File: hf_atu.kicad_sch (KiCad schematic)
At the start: 112 parts, among them J10 TO SWR_IN, J11 TO FILT_OUT, J7 To CTRL:ATU, J8 SWR_IN, J9 TO ANTENNA, K12 G6E, K13 G6E, K14 G6E, K15 G6E, K16 G6E, K17 G6E, K18 G6E, K19 G6E, K20 G6E, K21 G6E, K22 G6E, K23 G6E, K24 G6E, K25 G6E, K26 G6E, K27 G6E, K28 G6E, T1 Transformer_1P_SS, U10 74HC596, U11 ULN2803A, U6 74HC596, U7 ULN2803A, U8 74HC596, U9 ULN2803A

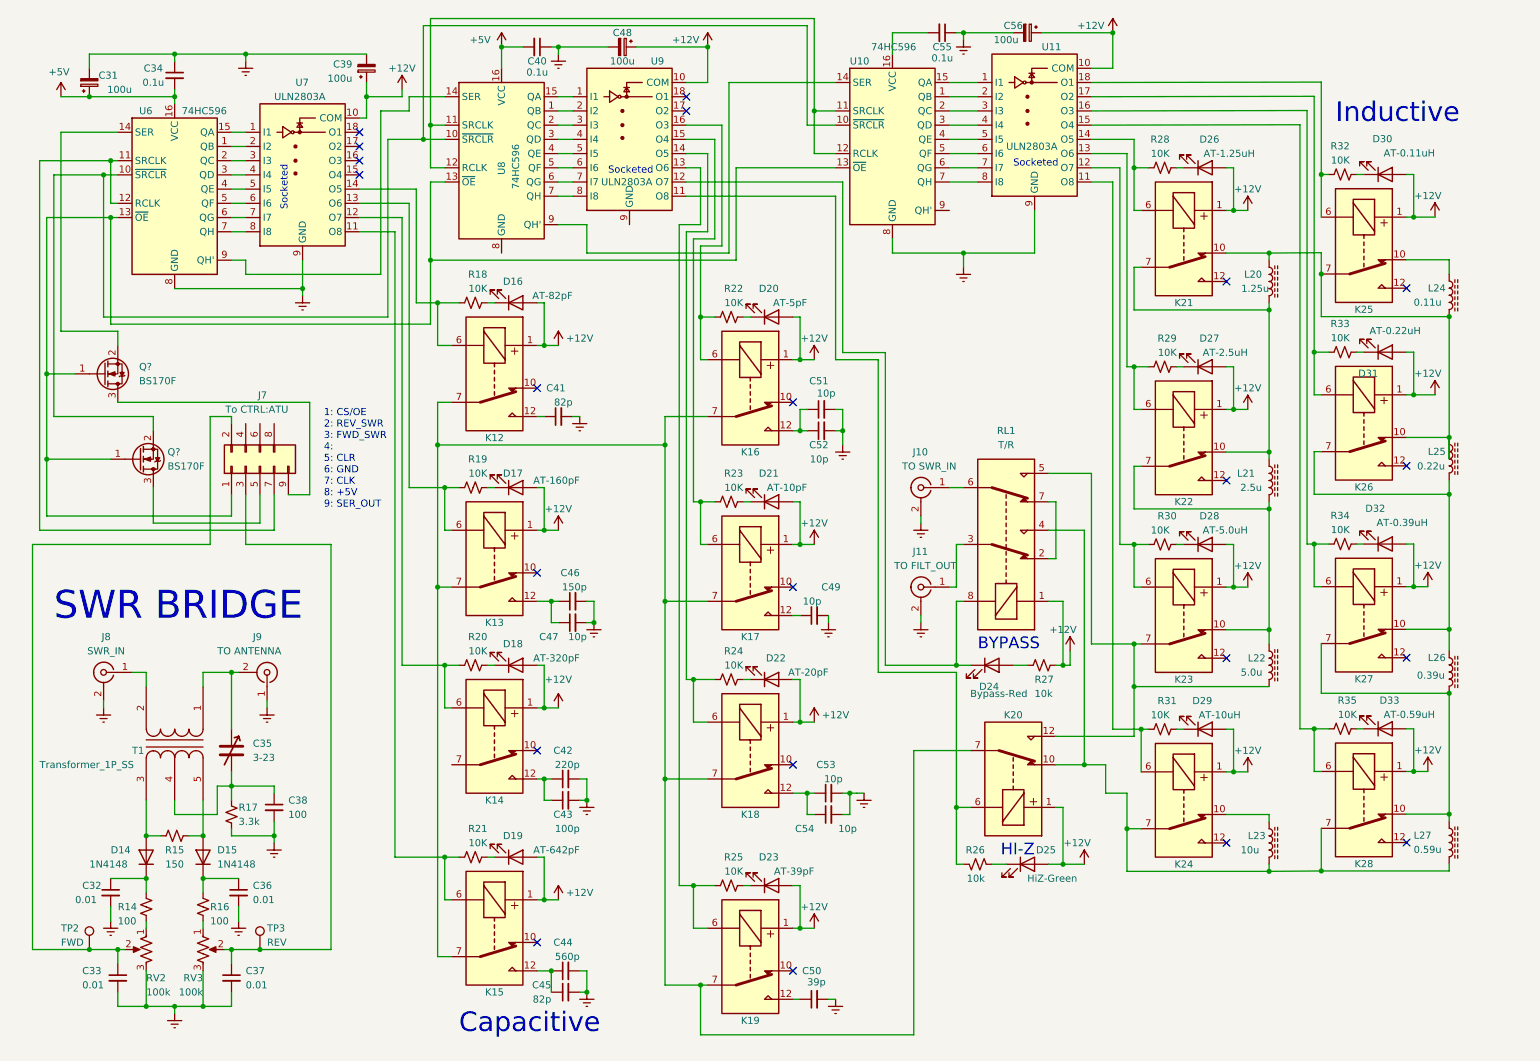
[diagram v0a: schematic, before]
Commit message: Replaced 74hc596 parts with mcp23017 and mcp23008 parts to simplify routing and reduce external parts count.
Added interface connectors for eventualy VHF (6m/2m/1.25m) RF path board.

Attempted to create some sort of documentations...
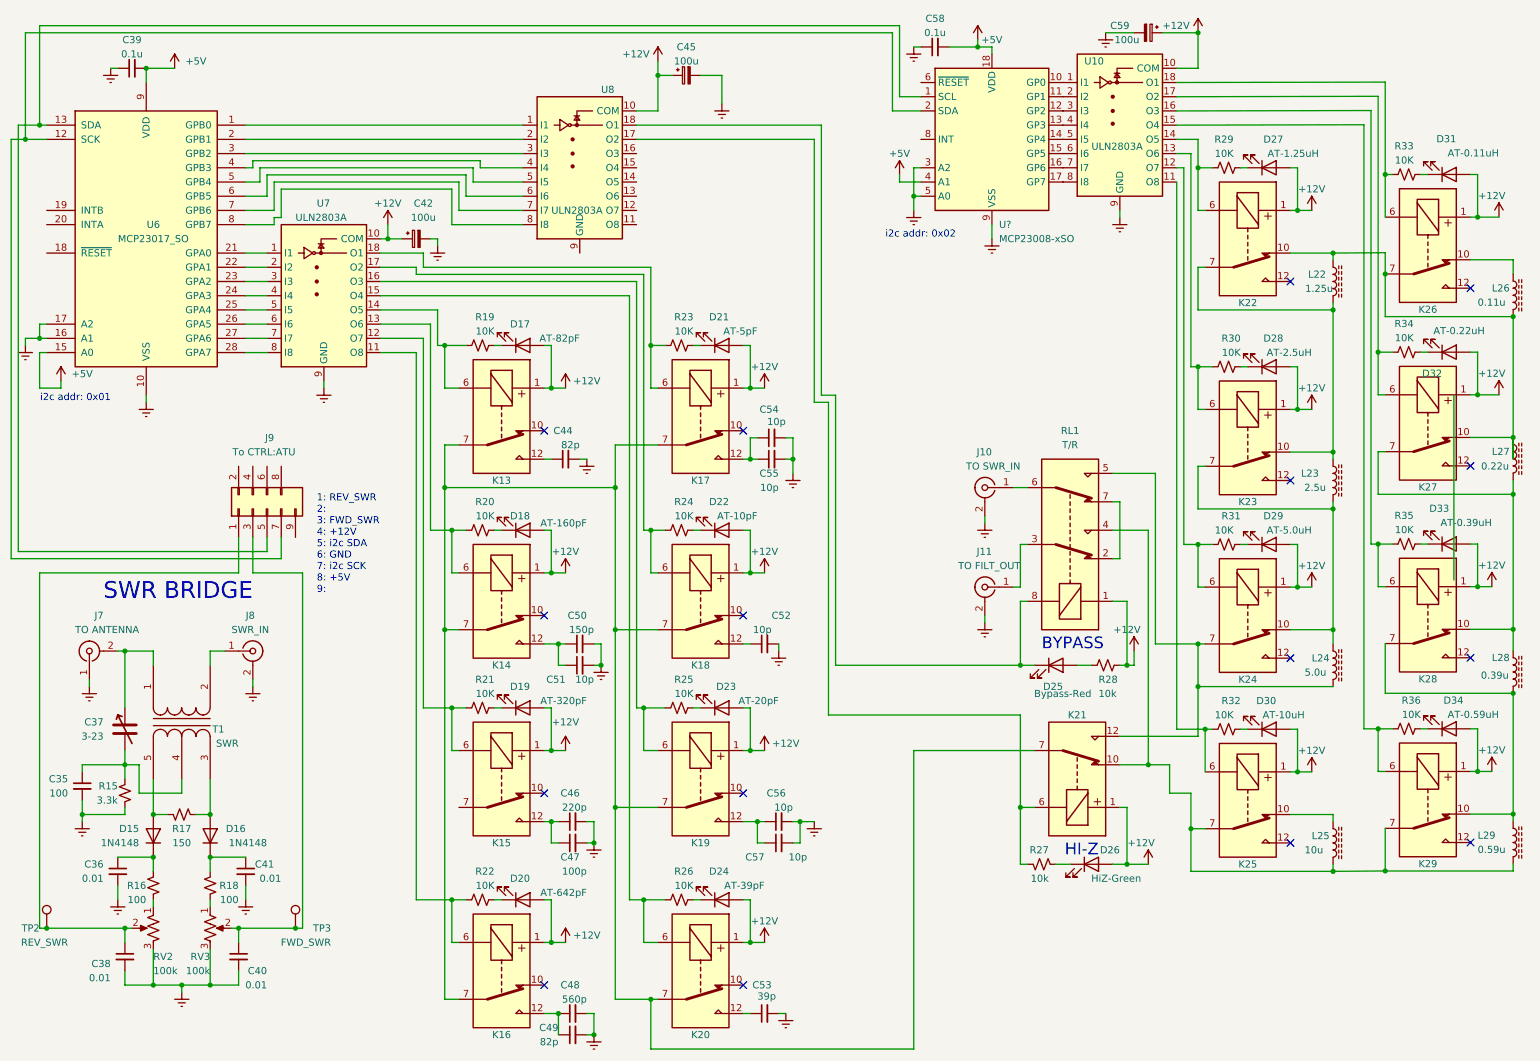
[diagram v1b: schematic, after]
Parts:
- removed C31: 100u, symbol Device:C_Polarized_Small
- removed C34, C40, C55: 0.1u, Capacitor_THT:C_Disc_D4.7mm_W2.5mm_P5.00mm, symbol Device:C_Small
- removed Q? (x2): BS170F, Package_TO_SOT_SMD:SOT-23, symbol Transistor_FET:BS170F
- removed U10, U6, U8: 74HC596, Package_SO:TSSOP-16_4.4x5mm_P0.65mm, symbol 74xx:74HC596
- added C39, C58: 0.1u, Capacitor_THT:C_Disc_D4.7mm_W2.5mm_P5.00mm, symbol Device:C_Small
- added U6: MCP23017_SO, Package_SO:SOIC-28W_7.5x17.9mm_P1.27mm, symbol Interface_Expansion:MCP23017_SO
- added U?: MCP23008-xSO, Package_SO:SOIC-18W_7.5x11.6mm_P1.27mm, symbol Interface_Expansion:MCP23008-xSO
- T1: value Transformer_1P_SS -> SWR
- TP2: renamed from TP3; value REV -> REV_SWR
- TP3: renamed from TP2; value FWD -> FWD_SWR
- renumbered C38 to C35, C35 to C37, C37 to C38, C33 to C40, C32 to C41, C39 to C42, C41 to C44, C48 to C45, C42 to C46, C43 to C47, C44 to C48, C45 to C49, C46 to C50, C47 to C51, C49 to C52, C50 to C53, C51 to C54, C52 to C55, C53 to C56, C54 to C57, C56 to C59, D14 to D16, D16 to D17, D17 to D18, D18 to D19, D19 to D20, D20 to D21, D21 to D22, D22 to D23, D23 to D24, D24 to D25, D25 to D26, D26 to D27, D27 to D28, D28 to D29, D29 to D30, D30 to D31, D31 to D32, D32 to D33, D33 to D34, J9 to J7, J7 to J9, K12 to K13, K13 to K14, K14 to K15, K15 to K16, K16 to K17, K17 to K18, K18 to K19, K19 to K20, K20 to K21, K21 to K22, K22 to K23, K23 to K24, K24 to K25, K25 to K26, K26 to K27, K27 to K28, K28 to K29, L20 to L22, L21 to L23, L22 to L24, L23 to L25, L24 to L26, L25 to L27, L26 to L28, L27 to L29, R17 to R15, R15 to R17, R14 to R18, R18 to R19, R19 to R20, R20 to R21, R21 to R22, R22 to R23, R23 to R24, R24 to R25, R25 to R26, R26 to R27, R27 to R28, R28 to R29, R29 to R30, R30 to R31, R31 to R32, R32 to R33, R33 to R34, R34 to R35, R35 to R36, RV3 to RV2, RV2 to RV3, U11 to U10, U9 to U8
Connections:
- net +5V: now also C39.2, C58.2, U6.15 (A0), U6.9 (VDD), U?.18 (VDD), U?.4 (A1)
- net Earth: now also C39.1, C58.1, U6.10 (VSS), U6.16 (A1), U6.17 (A2), U?.3 (A2), U?.5 (A0), U?.9 (VSS)
- net at K21.6, R27.1: now also U8.17 (O2); no longer U8.11 (O8)
- net at C40.1, RV3.2, TP3.1: now also J9.3 (Pin_3); no longer J9.2 (Pin_2)
- net at D25.1 (K), RL1.8: now also U8.18 (O1); no longer U8.12 (O7)
- net at U10.1 (I1): now also U?.10 (GP0)
- net at U10.2 (I2): now also U?.11 (GP1)
- net at U10.3 (I3): now also U?.12 (GP2)
- net at U10.4 (I4): now also U?.13 (GP3)
- net at U10.5 (I5): now also U?.14 (GP4)
- net at U10.6 (I6): now also U?.15 (GP5)
- net at U10.7 (I7): now also U?.16 (GP6)
- net at U10.8 (I8): now also U?.17 (GP7)
- net at K19.6, R25.1: now also U7.16 (O3); no longer U8.14 (O5)
- net at C38.1, RV2.2, TP2.1: now also J9.1 (Pin_1); no longer J9.3 (Pin_3)
- net at K20.6, R26.1: now also U7.15 (O4); no longer U8.13 (O6)
- net at J9.5 (Pin_5): now also U6.13 (SDA), U?.1 (SCL)
- net at J9.7 (Pin_7): now also U6.12 (SCK), U?.2 (SDA)
- net at U8.1 (I1): now also U6.1 (GPB0)
- net at K18.6, R24.1: now also U7.17 (O2); no longer U8.15 (O4)
- net at K17.6, R23.1: now also U7.18 (O1); no longer U8.16 (O3)
- net at U8.2 (I2): now also U6.2 (GPB1)
- net at U8.3 (I3): now also U6.3 (GPB2)
- net at U8.4 (I4): now also U6.4 (GPB3)
- net at U8.5 (I5): now also U6.5 (GPB4)
- net at U8.6 (I6): now also U6.6 (GPB5)
- net at U8.7 (I7): now also U6.7 (GPB6)
- net at U8.8 (I8): now also U6.8 (GPB7)
- net at U7.2 (I2): now also U6.22 (GPA1)
- net at U7.1 (I1): now also U6.21 (GPA0)
- net at U7.3 (I3): now also U6.23 (GPA2)
- net at U7.4 (I4): now also U6.24 (GPA3)
- net at U7.5 (I5): now also U6.25 (GPA4)
- net at U7.6 (I6): now also U6.26 (GPA5)
- net at U7.7 (I7): now also U6.27 (GPA6)
- net at U7.8 (I8): now also U6.28 (GPA7)
- no-connect marks 22 -> 16
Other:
- note added: "1: REV_SWR 2: 3: FWD_SWR 4: +12V 5: i2c SDA 6: GND 7: i2c SCK 8: +5V 9:"
- note added: "i2c addr: 0x01"
- note added: "i2c addr: 0x02"
- note removed: "1: CS/OE 2: REV_SWR 3: FWD_SWR 4: 5: CLR 6: GND 7: CLK 8: +5V 9: SER_OUT"
- note removed: "Capacitive"
- note removed: "Inductive"
- note removed: "Socketed"
- moved on the sheet: C35, C36, C37, C38, C40, C41, C42, C44, C45, C46, C47, C48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

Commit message: cleanup of schematic and some initial firmware works...
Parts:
- removed D25: Bypass-Red, symbol Device:LED
- removed D26: HiZ-Green, symbol Device:LED
- removed J10: TO SWR_IN, symbol Connector:Conn_Coaxial
- removed K21: G6E, Relay_THT:Relay_SPDT_Omron_G6E, symbol Relay:G6E
- removed R27, R28: 10k, symbol Device:R_Small_US
- added D20, D21, D22, D27, D28, D29: LED, symbol Device:LED
- added D30: HiZ-Green, symbol Device:LED
- added D31: Bypass-Red, symbol Device:LED
- added J12: TO SWR_IN, symbol Connector:Conn_Coaxial
- added K22: G6E, Relay_THT:Relay_SPDT_Omron_G6E, symbol Relay:G6E
- added R22, R23, R24, R29, R30, R31: 10K, symbol Device:R_Small_US
- added R32, R33: 10k, symbol Device:R_Small_US
- J11: value TO FILT_OUT -> TO TX_FILT_OUT
- J9: renamed from J7; value TO ANTENNA -> SWR_OUT
- RL1: value T/R -> Bypass
- gave numbers to parts that had none: 1
- renumbered C35 to C40, C36 to C41, C37 to C42, C38 to C43, C39 to C44, C40 to C45, C41 to C46, C42 to C47, C44 to C48, C46 to C49, C47 to C50, C48 to C51, C49 to C52, C50 to C53, C51 to C54, C45 to C55, C52 to C56, C53 to C57, C54 to C58, C55 to C59, C56 to C60, C57 to C61, C58 to C62, C59 to C63, D15 to D14, D16 to D15, D17 to D16, D18 to D17, D19 to D18, D20 to D19, D21 to D23, D22 to D24, D23 to D25, D24 to D26, D27 to D32, D28 to D33, D29 to D34, D30 to D35, D32 to D36, D33 to D37, D34 to D38, D31 to D39, J9 to J10, K13 to K14, K14 to K15, K15 to K16, K16 to K17, K17 to K18, K18 to K19, K19 to K20, K20 to K21, K22 to K23, K23 to K24, K24 to K25, K25 to K26, K26 to K30, L22 to L31, L23 to L32, L24 to L33, L25 to L34, L27 to L35, L28 to L36, L29 to L37, L26 to L38, R15 to R14, R16 to R15, R17 to R16, R18 to R17, R19 to R18, R20 to R19, R21 to R20, R22 to R21, R23 to R25, R24 to R26, R25 to R27, R26 to R28, R29 to R34, R30 to R35, R31 to R36, R32 to R37, R34 to R38, R35 to R39, R36 to R40, R33 to R41, RV2 to RV1, RV3 to RV2, TP2 to TP1, TP3 to TP2, U6 to U4, U7 to U5, U8 to U6, U10 to U8
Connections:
- net +12V: now also D20.2 (A), D21.2 (A), D22.2 (A), D27.2 (A), D28.2 (A), D29.2 (A), D30.2 (A), K22.1, R33.1
- net Earth: now also J9.2 (Ext), U6.9 (GND), J12.2 (Ext); no longer J9.1 (In)
- net at K26.7, K29.7, L34.2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: now also RL1.5, K22.10; no longer RL1.4
- net at K25.7, L33.2: now also RL1.4, K22.12; no longer RL1.5
- net at U6.17 (O2): now also R23.1
- net at K14.7, K15.7, K17.7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: now also K16.7, K22.7
- net at RL1.3: now also J12.1 (In); no longer J11.1 (In)
- net at RL1.6: now also J11.1 (In)
- net at U6.18 (O1): now also R22.1; no longer RL1.8
- net at J10.5 (Pin_5), U4.13 (SDA): now also U7.2 (SDA); no longer U7.1 (SCL)
- net at J10.7 (Pin_7), U4.12 (SCK): now also U7.1 (SCL); no longer U7.2 (SDA)
- net at U6.11 (O8): now also RL1.8, D31.1 (K)
- net at U6.12 (O7): now also K22.6, R32.1
- net at U6.13 (O6): now also R31.1
- net at U6.14 (O5): now also R30.1
- net at U6.15 (O4): now also R29.1
- net at U6.16 (O3): now also R24.1
- net at C42.1, T1.1 (AA): now also J9.1 (In); no longer J9.2 (Ext)
- new net: D27.1 (K), R29.2
- new net: D31.2 (A), R33.2
- new net: D20.1 (K), R22.2
- new net: D28.1 (K), R30.2
- new net: D30.1 (K), R32.2
- new net: D29.1 (K), R31.2
- new net: D21.1 (K), R23.2
- new net: D22.1 (K), R24.2
- no-connect marks 16 -> 26
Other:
- note added: "L/C values derived from published LDG AT-11 manual. RF path designed to minimize # of relays needed Board interconnections via SMA connections."
- moved on the sheet: C40, C41, C42, C43, C44, C45, C46, C47, C48, C49, C50, C51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

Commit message: cleanup
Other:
- note added: "status lights"
- moved on the sheet: C47, C55, D20, D21, D22, D27, D28, D29, R22, R23, R24, R29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

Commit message: cleanup and trying to implement stubs for future features
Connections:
- net Earth: no longer C58.2
- net at C58.1, K18.12: no longer C59.1
- new net: C58.2, C59.1
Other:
- moved on the sheet: C58, C59
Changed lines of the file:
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@@
   (junction (at 276.0236 145.9774) (diameter 0) (color 194 0 0 1)
   )
-  (junction (at 153.67 88.9) (diameter 0) (color 194 0 194 1)
-  )
   (junction (at 250.19 163.83) (diameter 0) (color 132 0 132 1)
   )
@@
   (junction (at 110.49 140.97) (diameter 0) (color 194 0 0 1)
   )
-  (junction (at 146.05 88.9) (diameter 0) (color 194 0 194 1)
-  )
   (junction (at 203.2 132.08) (diameter 0) (color 194 0 0 1)
   )
@@
     (stroke (width 0) (type dash) (color 132 0 132 1))
   )
-  (wire (pts (xy 146.05 85.09) (xy 146.05 88.9))
-    (stroke (width 0) (type dash) (color 194 0 194 1))
-  )
   (wire (pts (xy 276.0248 46.928) (xy 278.1312 47.0006))
     (stroke (width 0) (type default) (color 194 0 0 1))
@@
     (stroke (width 0) (type dash) (color 132 0 132 1))
   )
-  (wire (pts (xy 146.05 85.09) (xy 147.32 85.09))
+  (wire (pts (xy 144.78 88.9) (xy 147.32 88.9))
     (stroke (width 0) (type dash) (color 194 0 194 1))
   )
@@
     (stroke (width 0) (type dash) (color 132 0 132 1))
   )
-  (wire (pts (xy 152.4 88.9) (xy 153.67 88.9))
+  (wire (pts (xy 158.75 88.9) (xy 160.02 88.9))
     (stroke (width 0) (type dash) (color 194 0 194 1))
   )
@@
     (stroke (width 0) (type default))
   )
-  (wire (pts (xy 146.05 88.9) (xy 147.32 88.9))
-    (stroke (width 0) (type dash) (color 194 0 194 1))
-  )
   (wire (pts (xy 146.05 133.35) (xy 146.05 140.97))
     (stroke (width 0) (type default) (color 194 0 0 1))
@@
     (stroke (width 0) (type default))
   )
-  (wire (pts (xy 153.67 88.9) (xy 153.67 91.44))
+  (wire (pts (xy 160.02 88.9) (xy 160.02 91.44))
     (stroke (width 0) (type dash) (color 194 0 194 1))
   )
@@
     (stroke (width 0) (type default) (color 194 0 0 1))
   )
-  (wire (pts (xy 153.67 85.09) (xy 152.4 85.09))
+  (wire (pts (xy 153.67 88.9) (xy 152.4 88.9))
     (stroke (width 0) (type dash) (color 194 0 194 1))
   )
@@
     (stroke (width 0) (type dash) (color 132 0 132 1))
   )
-  (wire (pts (xy 153.67 88.9) (xy 153.67 85.09))
-    (stroke (width 0) (type dash) (color 194 0 194 1))
-  )
   (wire (pts (xy 223.52 105.41) (xy 226.06 105.41))
     (stroke (width 0) (type dot))
@@
     (stroke (width 0) (type default) (color 194 0 0 1))
   )
-  (wire (pts (xy 144.78 88.9) (xy 146.05 88.9))
-    (stroke (width 0) (type dash) (color 194 0 194 1))
-  )
   (wire (pts (xy 276.0236 145.9774) (xy 278.5636 145.9774))
     (stroke (width 0) (type default) (color 194 0 0 1))
@@
     )
   )
-  (symbol (lib_id "Device:C_Small") (at 149.86 88.9 90) (unit 1)
+  (symbol (lib_id "Device:C_Small") (at 156.21 88.9 90) (unit 1)
     (in_bom yes) (on_board yes) (dnp no)
-    (property "Reference" "C59" (at 151.13 91.44 90)
+    (property "Reference" "C59" (at 157.48 91.44 90)
       (effects (font (size 1.27 1.27)) (justify left))
     )
-    (property "Value" "10p" (at 151.13 93.98 90)
+    (property "Value" "10p" (at 157.48 93.98 90)
       (effects (font (size 1.27 1.27)) (justify left))
     )
-    (property "Footprint" "" (at 149.86 88.9 0)
+    (property "Footprint" "" (at 156.21 88.9 0)
       (effects (font (size 1.27 1.27)) hide)
     )
-    (property "Datasheet" "~" (at 149.86 88.9 0)
+    (property "Datasheet" "~" (at 156.21 88.9 0)
       (effects (font (size 1.27 1.27)) hide)
     )
@@
     )
   )
-  (symbol (lib_id "power:Earth") (at 153.67 91.44 0) (unit 1)
+  (symbol (lib_id "power:Earth") (at 160.02 91.44 0) (unit 1)
     (in_bom yes) (on_board yes) (dnp no) (fields_autoplaced)
-    (property "Reference" "#PWR078" (at 153.67 97.79 0)
+    (property "Reference" "#PWR078" (at 160.02 97.79 0)
       (effects (font (size 1.27 1.27)) hide)
     )
-    (property "Value" "Earth" (at 153.67 95.25 0)
+    (property "Value" "Earth" (at 160.02 95.25 0)
       (effects (font (size 1.27 1.27)) hide)
     )
-    (property "Footprint" "" (at 153.67 91.44 0)
+    (property "Footprint" "" (at 160.02 91.44 0)
       (effects (font (size 1.27 1.27)) hide)
     )
-    (property "Datasheet" "~" (at 153.67 91.44 0)
+    (property "Datasheet" "~" (at 160.02 91.44 0)
       (effects (font (size 1.27 1.27)) hide)
     )
@@
     )
   )
-  (symbol (lib_id "Device:C_Small") (at 149.86 85.09 90) (unit 1)
+  (symbol (lib_id "Device:C_Small") (at 149.86 88.9 90) (unit 1)
     (in_bom yes) (on_board yes) (dnp no)
-    (property "Reference" "C58" (at 151.13 80.01 90)
+    (property "Reference" "C58" (at 151.13 91.44 90)
       (effects (font (size 1.27 1.27)) (justify left))
     )
-    (property "Value" "10p" (at 152.3818 82.211 90)
+    (property "Value" "10p" (at 152.3818 93.641 90)
       (effects (font (size 1.27 1.27)) (justify left))
     )
-    (property "Footprint" "" (at 149.86 85.09 0)
+    (property "Footprint" "" (at 149.86 88.9 0)
       (effects (font (size 1.27 1.27)) hide)
     )
-    (property "Datasheet" "~" (at 149.86 85.09 0)
+    (property "Datasheet" "~" (at 149.86 88.9 0)
       (effects (font (size 1.27 1.27)) hide)
     )
